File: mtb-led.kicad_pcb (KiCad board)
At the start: 2 copper layers, 120 x 50 mm, 58 parts, among them J7 AVR-ISP-6, J9 DEBUG, SW1 SW_Push, U1 ATmega328PB-A, U2 78M05, U3 TLC5940PWP, U4 TLC5940PWP, U5 MAX487E, Y1 14.7456 MHz

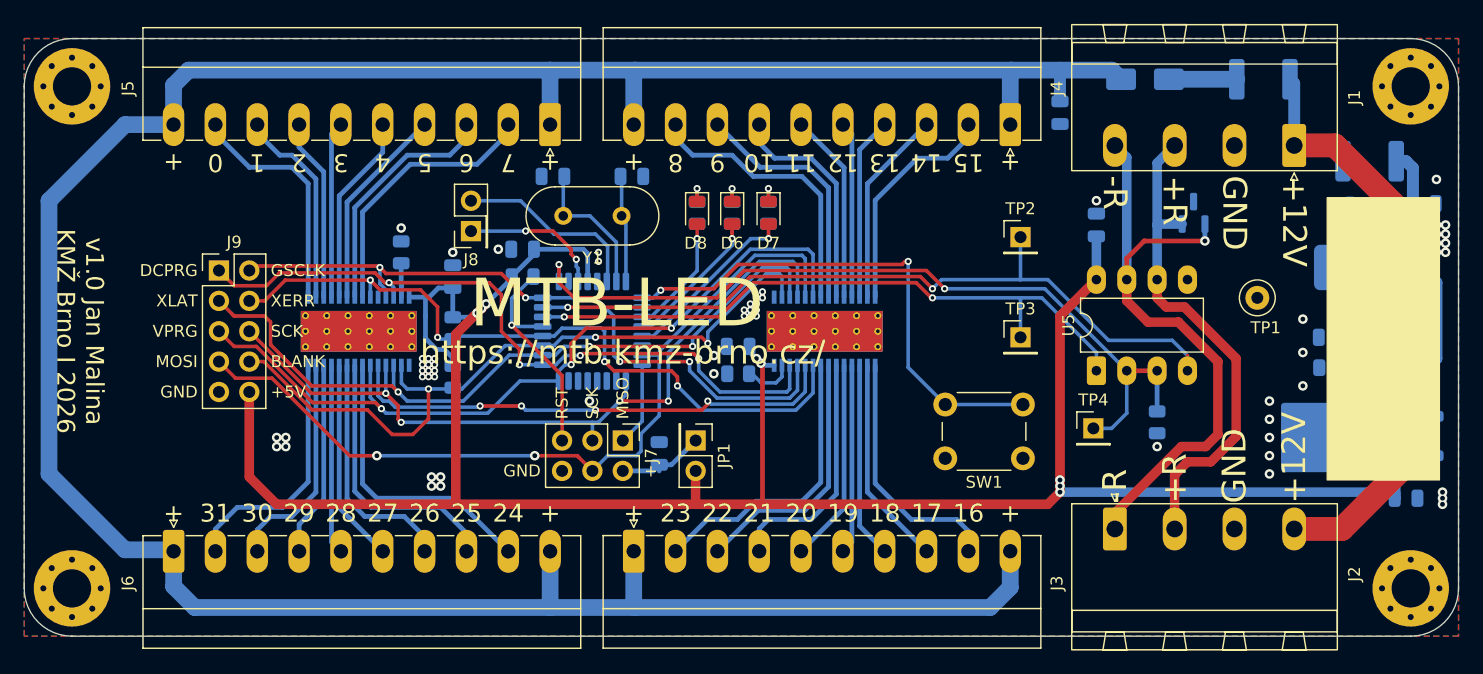
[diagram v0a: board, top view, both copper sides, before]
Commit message: PCB: resolve serious DRC errors.
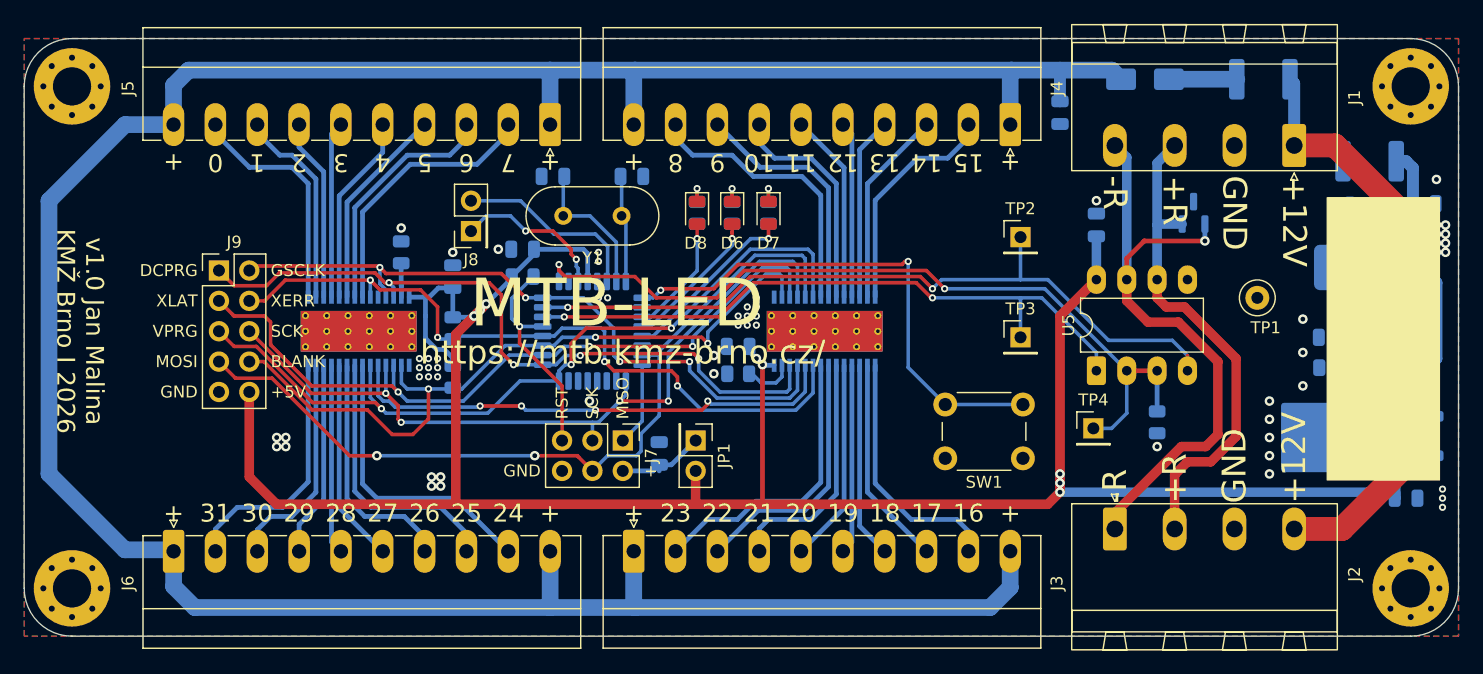
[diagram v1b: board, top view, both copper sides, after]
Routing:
- net /DEBUG1: track 12.0 -> 13.0 mm
- net /RST: track 19.0 -> 18.2 mm
- net /MTB-DE: track 68.2 -> 67.6 mm
- net /GSCLK: track 58.0 -> 57.4 mm
- net +5V: track 200.2 -> 200.7 mm
- net GND: vias 67 -> 64

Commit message: Add JLCPCB tooling holes.
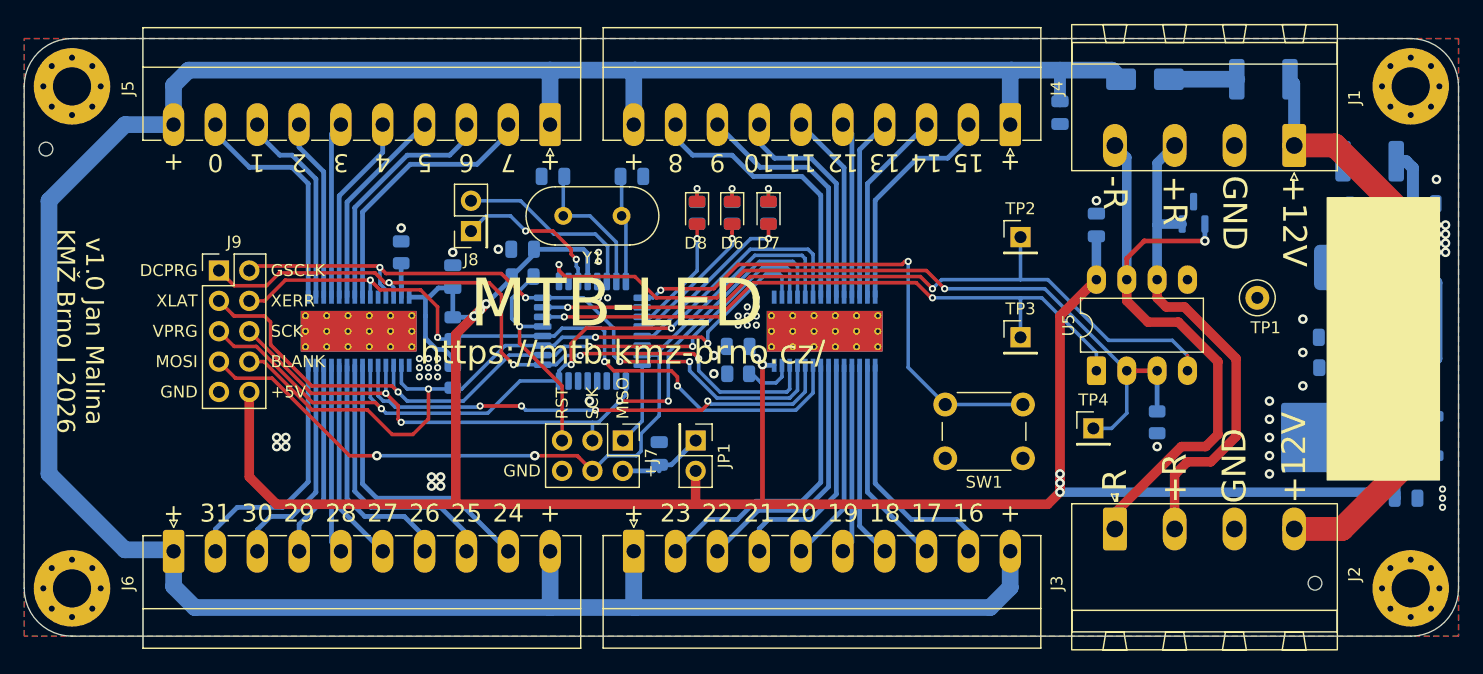
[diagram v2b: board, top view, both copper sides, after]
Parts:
- added ?: , , F.Cu at (190.0, 115.6)
- added REF**: ToolingHole_1.152mm, MountingHole:ToolingHole_1.152mm, F.Cu at (83.8, 79.2)
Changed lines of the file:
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@@
 		)
+	)
+	(footprint "MountingHole:ToolingHole_1.152mm"
+		(layer "F.Cu")
+		(at 83.82 79.248)
+		(descr "Tooling Hole 1.152mm, 1.3mm solder mask, JLCPCB specification, https://jlcpcb.com/help/article/How-to-add-tooling-holes-for-PCB-assembly-order")
+		(tags "mounting")
+		(property "Reference" "REF**"
+			(at 0 -1.5 0)
+			(layer "F.SilkS")
+			(hide yes)
+			(effects
+				(font
+					(size 1 1)
+					(thickness 0.15)
+				)
+			)
+		)
+		(property "Value" "ToolingHole_1.152mm"
+			(at 0 1.6 0)
+			(layer "F.Fab")
+			(hide yes)
+			(effects
+				(font
+					(size 1 1)
+					(thickness 0.15)
+				)
+			)
+		)
+		(property "Datasheet" ""
+			(at 0 0 0)
+			(unlocked yes)
+			(layer "F.Fab")
+			(hide yes)
+			(effects
+				(font
+					(size 1.27 1.27)
+					(thickness 0.15)
+				)
+			)
+		)
+		(property "Description" ""
+			(at 0 0 0)
+			(unlocked yes)
+			(layer "F.Fab")
+			(hide yes)
+			(effects
+				(font
+					(size 1.27 1.27)
+					(thickness 0.15)
+				)
+			)
+		)
+		(attr exclude_from_pos_files exclude_from_bom)
+		(fp_circle
+			(center 0 0)
+			(end 0.7 0)
+			(stroke
+				(width 0.05)
+				(type solid)
+			)
+			(fill no)
+			(layer "F.CrtYd")
+		)
+		(fp_text user "${REFERENCE}"
+			(at 0 0 0)
+			(layer "F.Fab")
+			(effects
+				(font
+					(size 1 1)
+					(thickness 0.15)
+				)
+			)
+		)
+		(pad "" np_thru_hole circle
+			(at 0 0)
+			(size 1.152 1.152)
+			(drill 1.152)
+			(layers "*.Cu" "*.Mask")
+			(solder_mask_margin 0.074)
+		)
+		(zone
+			(net 0)
+			(net_name "")
+			(layers "F.Cu" "B.Cu")
+			(hatch edge 0.5)
+			(connect_pads
+				(clearance 0)
+			)
+			(min_thickness 0.25)
+			(filled_areas_thickness no)
+			(keepout
+				(tracks not_allowed)
+				(vias allowed)
+				(pads allowed)
+				(copperpour not_allowed)
+				(footprints not_allowed)
+			)
+			(placement
+				(enabled no)
+				(sheetname "")
+			)
+			(fill
+				(thermal_gap 0.5)
+				(thermal_bridge_width 0.5)
+			)
+			(polygon
+				(pts
+					(xy 84.52 79.248) (xy 84.499659 79.080479) (xy 84.439819 78.922694) (xy 84.343958 78.783814) (xy 84.217645 78.671911)
+					(xy 84.068223 78.593489) (xy 83.904376 78.553104) (xy 83.735624 78.553104) (xy 83.571777 78.593489)
+					(xy 83.422355 78.671911) (xy 83.296042 78.783814) (xy 83.200181 78.922694) (xy 83.140341 79.080479)
+					(xy 83.12 79.248) (xy 83.140341 79.415521) (xy 83.200181 79.573306) (xy 83.296042 79.712186) (xy 83.422355 79.824089)
+					(xy 83.571777 79.902511) (xy 83.735624 79.942896) (xy 83.904376 79.942896) (xy 84.068223 79.902511)
+					(xy 84.217645 79.824089) (xy 84.343958 79.712186) (xy 84.439819 79.573306) (xy 84.499659 79.415521)
+				)
+			)
+		)
+		(embedded_fonts no)
 	)
 	(footprint "Connector_PinHeader_2.54mm:PinHeader_1x01_P2.54mm_Vertical"
@@
 		)
 	)
+	(footprint ""
+		(layer "F.Cu")
+		(at 189.992 115.57)
+		(property "Reference" ""
+			(at 0 0 0)
+			(layer "F.SilkS")
+			(effects
+				(font
+					(size 1.27 1.27)
+					(thickness 0.15)
+				)
+			)
+		)
+		(property "Value" ""
+			(at 0 0 0)
+			(layer "F.Fab")
+			(effects
+				(font
+					(size 1.27 1.27)
+					(thickness 0.15)
+				)
+			)
+		)
+		(property "Datasheet" ""
+			(at 0 0 0)
+			(layer "F.Fab")
+			(hide yes)
+			(effects
+				(font
+					(size 1.27 1.27)
+					(thickness 0.15)
+				)
+			)
+		)
+		(property "Description" ""
+			(at 0 0 0)
+			(layer "F.Fab")
+			(hide yes)
+			(effects
+				(font
+					(size 1.27 1.27)
+					(thickness 0.15)
+				)
+			)
+		)
+		(pad "" np_thru_hole circle
+			(at 0 0)
+			(size 1.152 1.152)
+			(drill 1.152)
+			(layers "*.Cu" "*.Mask")
+			(solder_mask_margin 0.074)
+		)
+		(embedded_fonts no)
+	)
 	(footprint "Connector_PinHeader_2.54mm:PinHeader_2x05_P2.54mm_Vertical"

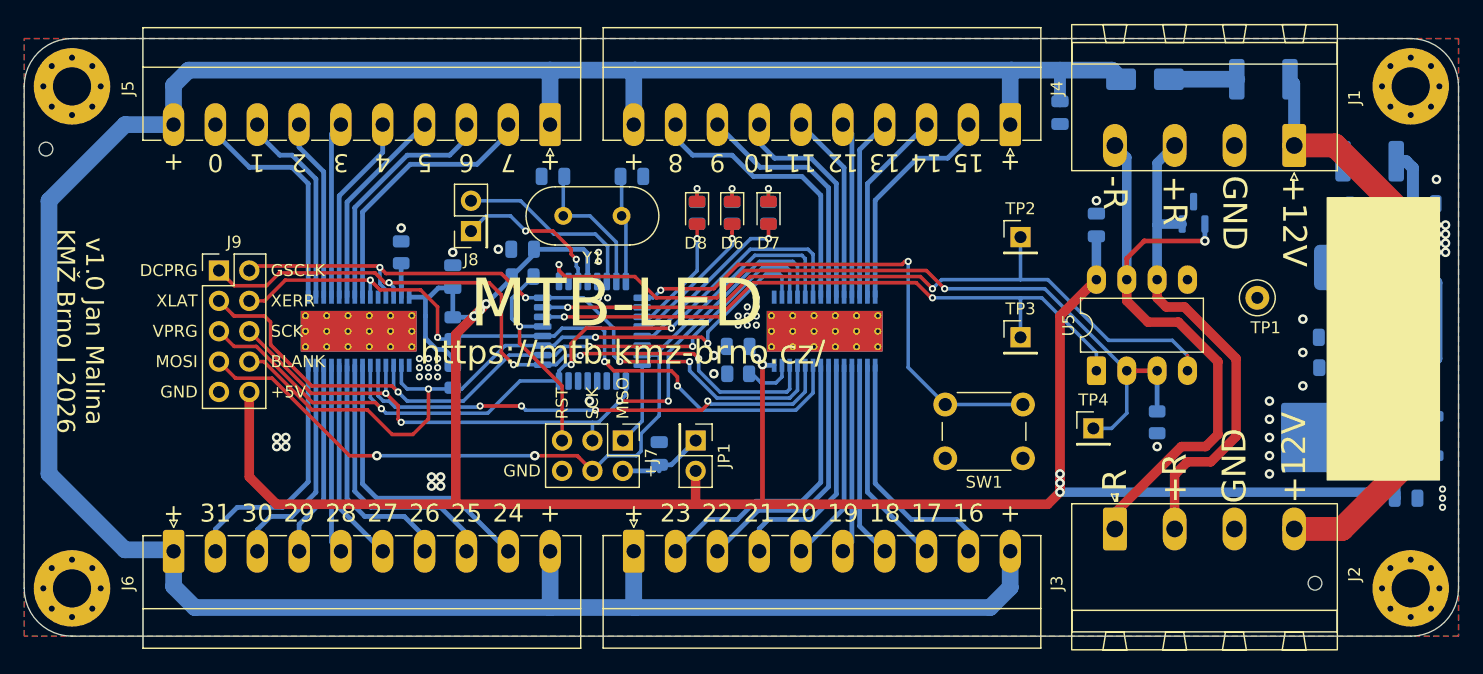
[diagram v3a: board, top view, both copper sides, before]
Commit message: Add vias.
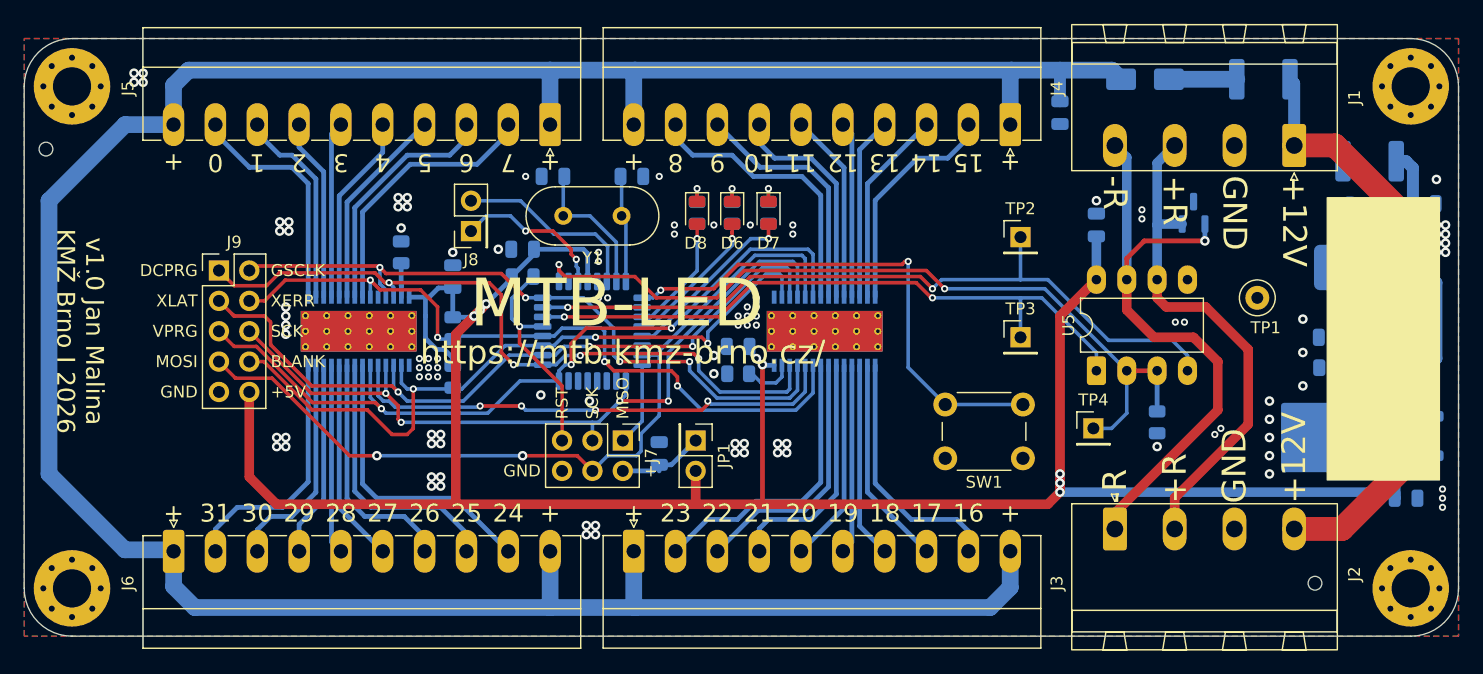
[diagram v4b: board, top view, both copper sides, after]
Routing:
- net /BLANK: track 60.9 -> 60.1 mm
- net /BUS+: track 41.7 -> 42.5 mm
- net /BUS-: track 52.2 -> 51.5 mm
- net +5V: track 200.7 -> 201.5 mm
- net GND: vias 64 -> 111
